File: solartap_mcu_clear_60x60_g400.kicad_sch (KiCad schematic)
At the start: 27 parts, among them J1 USB_C_Receptacle_USB2.0_16P, U1 nRF52832-QFxx, U2 RS3002-3.3SYF5, Y1 32Mhz

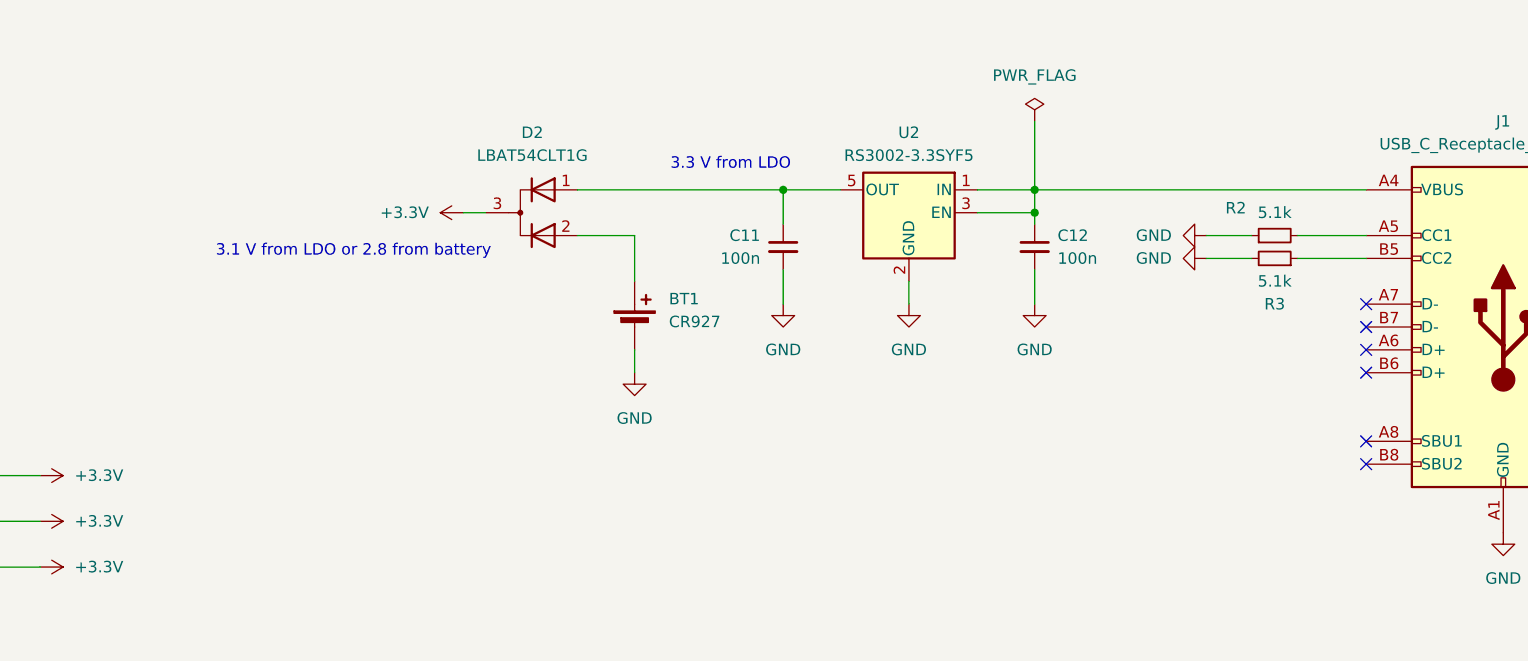
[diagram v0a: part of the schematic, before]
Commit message: Переделали схему под аккомулятор + добавили его чарджер. rev.F
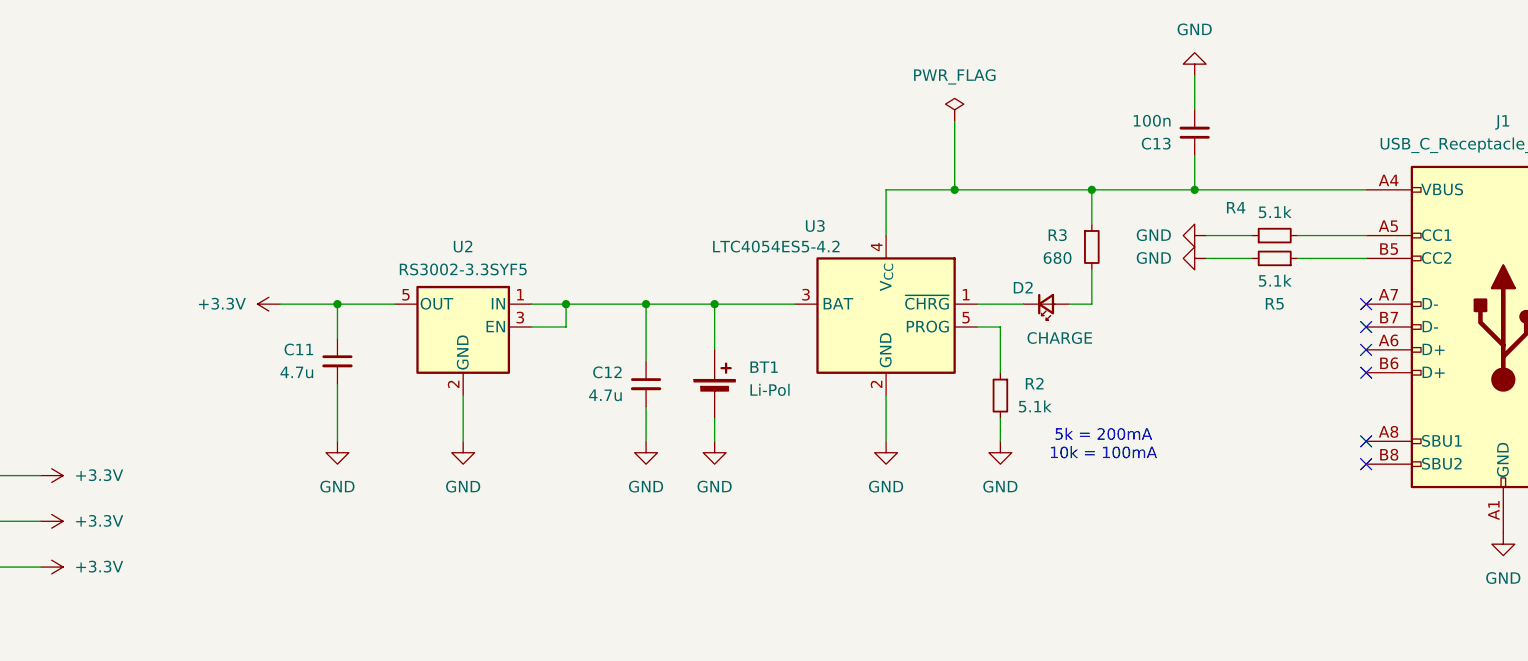
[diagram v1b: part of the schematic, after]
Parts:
- removed D2: LBAT54CLT1G, Package_TO_SOT_SMD:SOT-23-3, symbol Device:D_Dual_CommonCathode_AAK_Parallel
- added C12: 4.7u, Capacitor_SMD:C_0805_2012Metric, symbol Device:C_Small
- added D2: CHARGE, LED_SMD:LED_0805_2012Metric, symbol Device:LED_Small
- added R2: 5.1k, Resistor_SMD:R_0805_2012Metric, symbol Device:R_Small
- added R3: 680, Resistor_SMD:R_0805_2012Metric, symbol Device:R_Small
- added U3: LTC4054ES5-4.2, Package_TO_SOT_SMD:TSOT-23-5, symbol Battery_Management:LTC4054ES5-4.2
- BT1: value CR927 -> Li-Pol; footprint Battery:CR927 -> Battery:li-pol
- C11: value 100n -> 4.7u
- TP1, TP2, TP3, TP4, TP5: footprint TestPoint:TestPoint_Pad_D2.0mm -> TestPoint:TestPoint_Keystone_5015_Micro-Minature
- renumbered C12 to C13, R2 to R4, R3 to R5
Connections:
- net +3.3V: now also C11.1, U2.5 (OUT)
- net GND: now also C12.2, R2.2, U3.2 (GND)
- net at C13.1, J1.A4 (VBUS), J1.A9 (VBUS)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: now also R3.1, U3.4 (V_{CC}); no longer U2.1 (IN), U2.3 (EN)
- net at BT1.1 (+): now also U2.1 (IN), U2.3 (EN), C12.1, U3.3 (BAT)
- new net: D2.2 (A), R3.2
- new net: D2.1 (K), U3.1 (~{CHRG})
- new net: R2.1, U3.5 (PROG)
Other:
- note added: "5k = 200mA 10k = 100mA"
- note removed: "3.1 V from LDO or 2.8 from battery"
- note removed: "3.3 V from LDO"
- moved on the sheet: C11, C13, U2
